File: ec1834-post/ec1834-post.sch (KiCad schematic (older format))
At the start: 15 parts

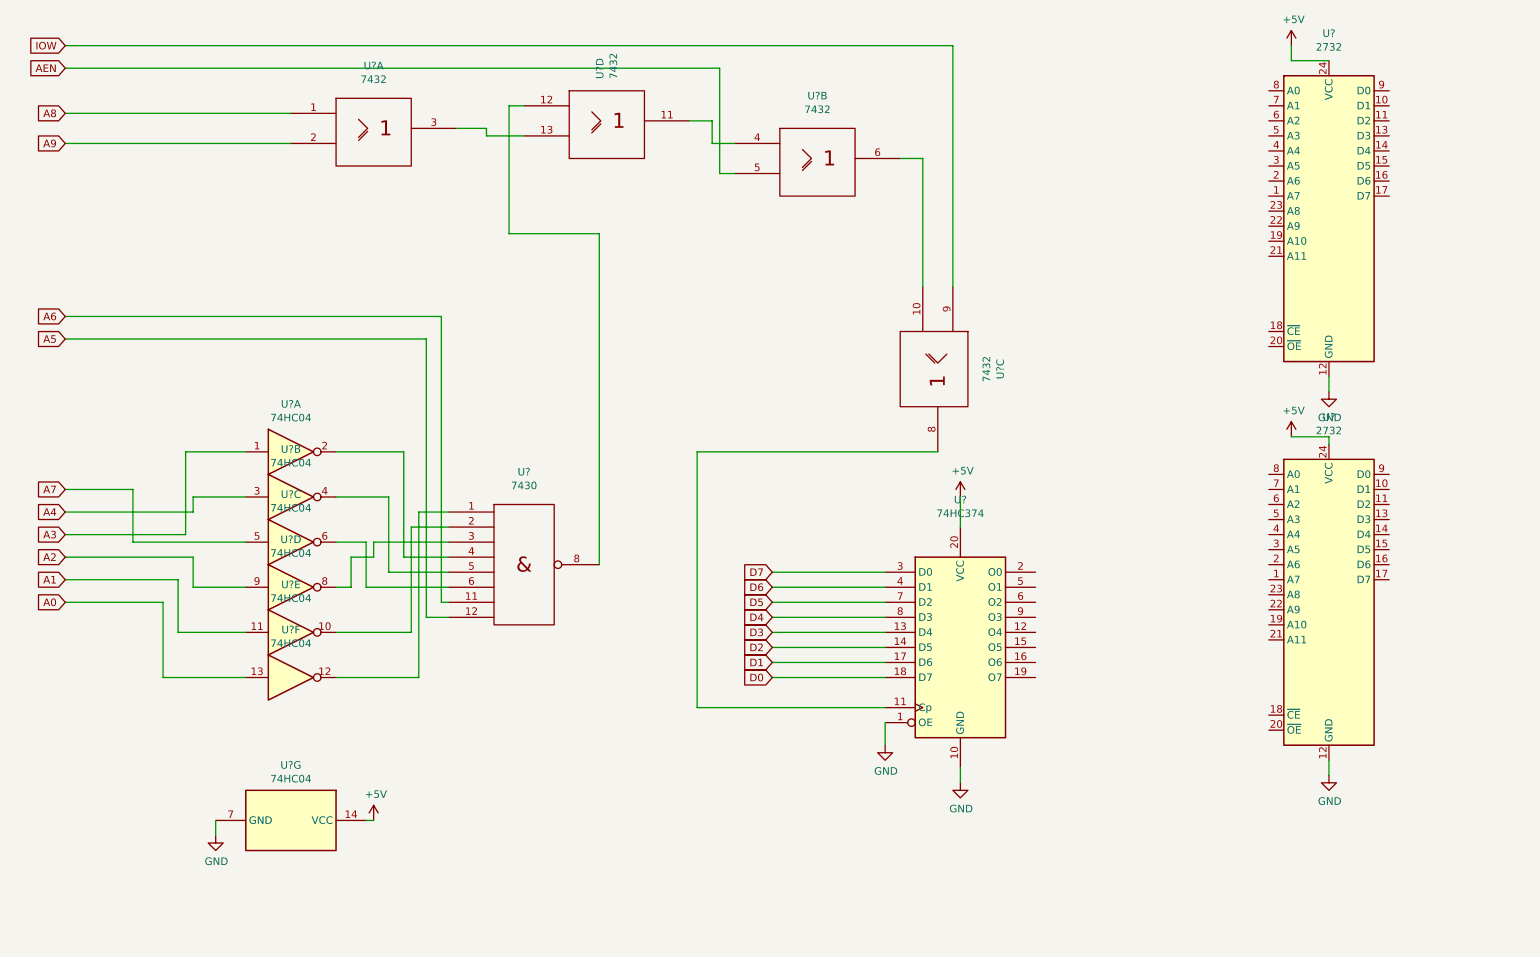
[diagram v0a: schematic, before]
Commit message: Schema completed Building PCB...
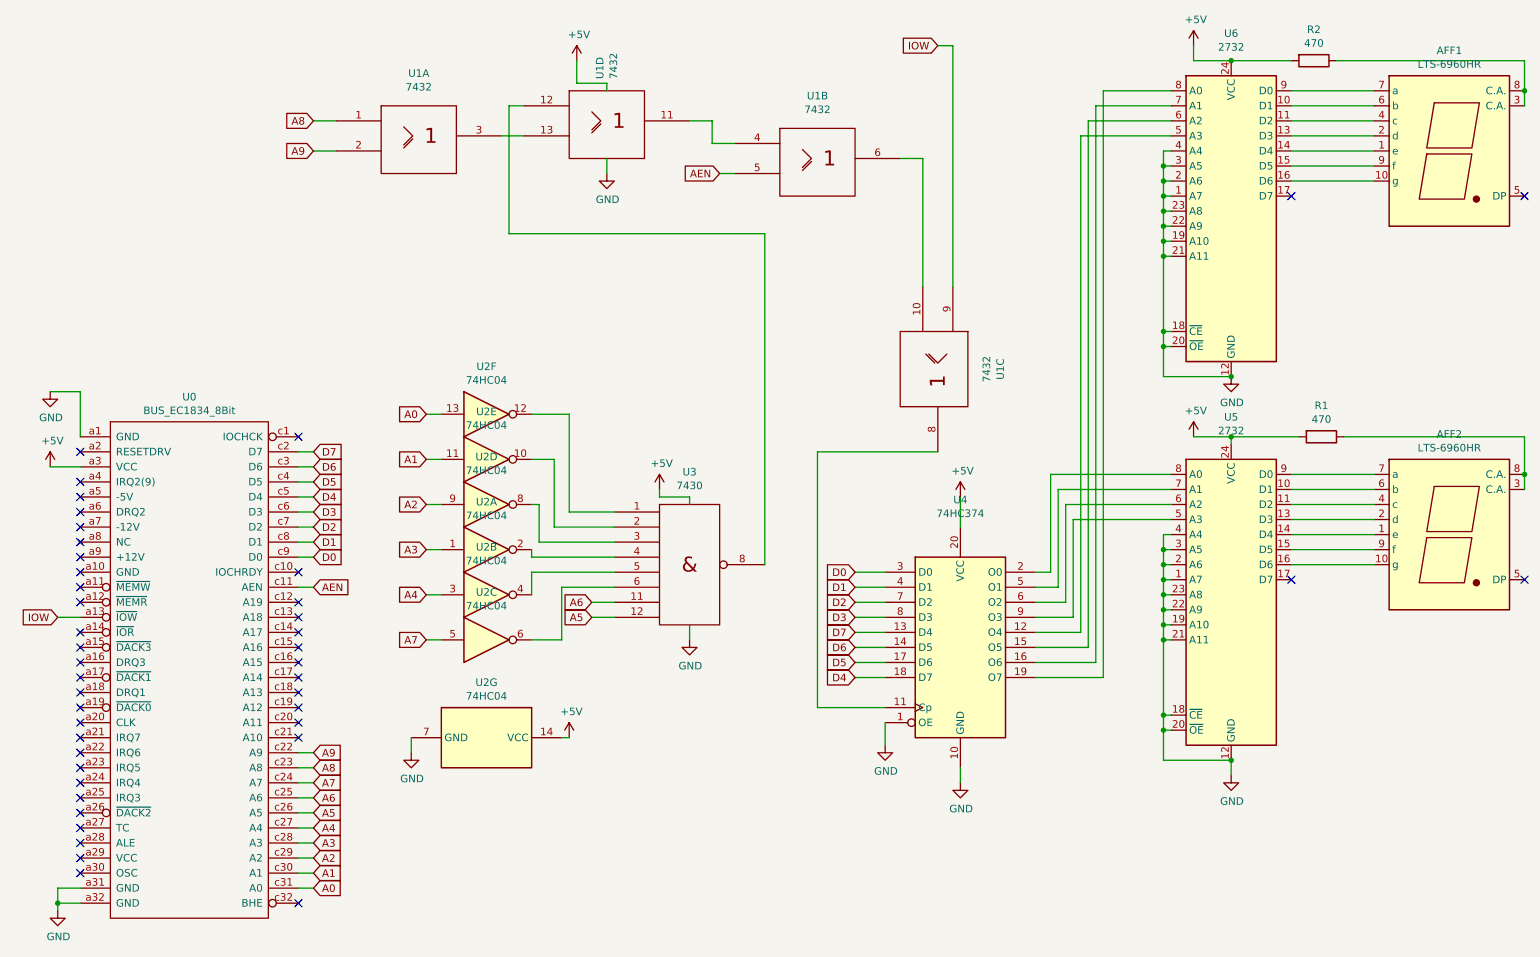
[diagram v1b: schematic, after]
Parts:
- added AFF1, AFF2: LTS-6960HR, Display_7Segment:7SegmentLED_LTS6760_LTS6780, symbol Display_Character:LTS-6960HR
- added R1, R2: 470, Resistor_THT:R_Axial_DIN0309_L9.0mm_D3.2mm_P12.70mm_Horizontal, symbol Device:R
- added U0: BUS_EC1834_8Bit, Connector_DIN:DIN41612_C_2x32_Male_Horizontal_THT, symbol ec1834-post-lib:BUS_EC1834_8Bit
- U1, U2, U3: renamed from U?; footprint (none) -> Package_DIP:DIP-14_W10.16mm
- U4: renamed from U?; footprint (none) -> Package_DIP:DIP-20_W7.62mm
- gave numbers to parts that had none: 2
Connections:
- net Gnd is gone; now on net GND: U1.7 (Gnd), U1.7 (Gnd), U1.7 (Gnd), U1.7 (Gnd), U3.7 (Gnd)
- net Vcc is gone; now on net +5V: U1.14 (Vcc), U1.14 (Vcc), U1.14 (Vcc), U1.14 (Vcc), U3.14 (Vcc)
- net +5V: now also R1.2, R2.2, U0.a3 (VCC)
- net A0: now also U0.c31 (A0)
- net A1: now also U0.c30 (A1)
- net A2: now also U0.c29 (A2)
- net A3: now also U0.c28 (A3)
- net A4: now also U0.c27 (A4)
- net A5: now also U0.c26 (A5)
- net A6: now also U0.c25 (A6)
- net A7: now also U0.c24 (A7)
- net A8: now also U0.c23 (A8)
- net A9: now also U0.c22 (A9)
- net AEN: now also U0.c11 (AEN)
- net D0: now also U4.3 (D0), U0.c9 (D0); no longer U4.18 (D7)
- net D1: now also U4.4 (D1), U0.c8 (D1); no longer U4.17 (D6)
- net D2: now also U4.7 (D2), U0.c7 (D2); no longer U4.14 (D5)
- net D3: now also U4.8 (D3), U0.c6 (D3); no longer U4.13 (D4)
- net D4: now also U4.18 (D7), U0.c5 (D4); no longer U4.8 (D3)
- net D5: now also U4.17 (D6), U0.c4 (D5); no longer U4.7 (D2)
- net D6: now also U4.14 (D5), U0.c3 (D6); no longer U4.4 (D1)
- net D7: now also U4.13 (D4), U0.c2 (D7); no longer U4.3 (D0)
- net GND: now also U5.1 (A7), U5.18 (~CE), U5.19 (A10), U5.2 (A6), U5.20 (~OE), U5.21 (A11), U5.22 (A9), U5.23 (A8), U5.3 (A5), U5.4 (A4), U6.1 (A7), U6.18 (~CE), U6.19 (A10), U6.2 (A6), U6.20 (~OE), U6.21 (A11), U6.22 (A9), U6.23 (A8), U6.3 (A5), U6.4 (A4), U0.a1 (GND), U0.a31 (GND), U0.a32 (GND)
- net IOW: now also U0.a13 (~IOW)
- net at U4.12 (O4): now also U6.5 (A3)
- net at U4.15 (O5): now also U6.6 (A2)
- net at U4.16 (O6): now also U6.7 (A1)
- net at U4.19 (O7): now also U6.8 (A0)
- net at U4.2 (O0): now also U5.8 (A0)
- net at U4.5 (O1): now also U5.7 (A1)
- net at U4.6 (O2): now also U5.6 (A2)
- net at U4.9 (O3): now also U5.5 (A3)
- net at U6.10 (D1): now also AFF1.6 (b)
- net at U6.11 (D2): now also AFF1.4 (c)
- net at U6.13 (D3): now also AFF1.2 (d)
- net at U6.14 (D4): now also AFF1.1 (e)
- net at U6.15 (D5): now also AFF1.9 (f)
- net at U6.16 (D6): now also AFF1.10 (g)
- net at U6.9 (D0): now also AFF1.7 (a)
- net at U5.10 (D1): now also AFF2.6 (b)
- net at U5.11 (D2): now also AFF2.4 (c)
- net at U5.13 (D3): now also AFF2.2 (d)
- net at U5.14 (D4): now also AFF2.1 (e)
- net at U5.15 (D5): now also AFF2.9 (f)
- net at U5.16 (D6): now also AFF2.10 (g)
- net at U5.9 (D0): now also AFF2.7 (a)
- new net: AFF2.3 (C.A.), AFF2.8 (C.A.), R1.1
- new net: AFF1.3 (C.A.), AFF1.8 (C.A.), R2.1
- no-connect marks 0 -> 44
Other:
- moved on the sheet: U1A, U2A, U2B, U2C, U2D, U2E, U2F, U2G, U3, U5, U6

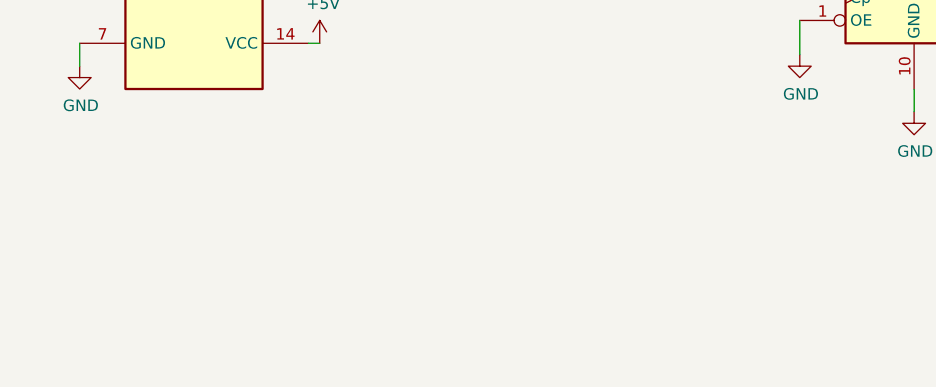
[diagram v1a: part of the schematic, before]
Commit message: Rework from CNC layout (which would be too close for 3018) to better layout for JLCPCB
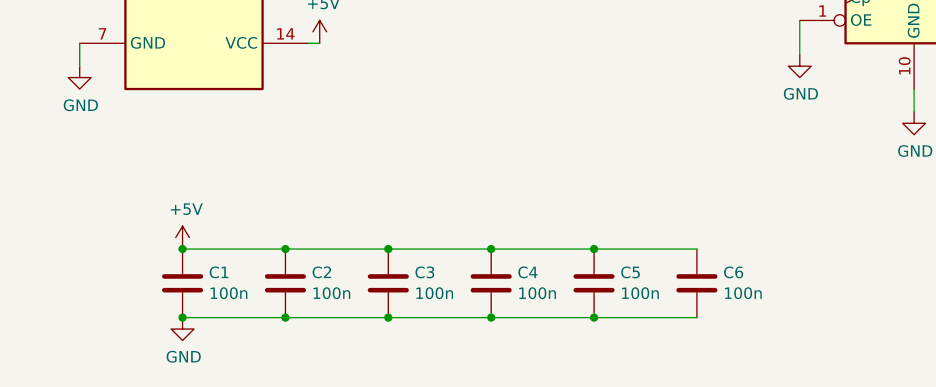
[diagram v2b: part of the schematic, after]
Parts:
- added C1, C2, C3: 100n, Capacitor_THT:C_Axial_L3.8mm_D2.6mm_P7.50mm_Horizontal, symbol Device:C
- added C4: 100n, Capacitor_THT:C_Axial_L5.1mm_D3.1mm_P7.50mm_Horizontal, symbol Device:C
- added C5, C6: 100n, Capacitor_THT:C_Axial_L5.1mm_D3.1mm_P10.00mm_Horizontal, symbol Device:C
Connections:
- net +5V: now also C1.1, C2.1, C3.1, C4.1, C5.1, C6.1
- net GND: now also C1.2, C2.2, C3.2, C4.2, C5.2, C6.2
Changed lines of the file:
@@
 Wire Wire Line
 	4900 5050 4900 5150
+$Comp
+L Device:C C1
+U 1 1 6249EDEF
+P 3500 6850
+F 0 "C1" H 3615 6896 50  0000 L CNN
+F 1 "100n" H 3615 6805 50  0000 L CNN
+F 2 "Capacitor_THT:C_Axial_L3.8mm_D2.6mm_P7.50mm_Horizontal" H 3538 6700 50  0001 C CNN
+F 3 "~" H 3500 6850 50  0001 C CNN
+	1    3500 6850
+	1    0    0    -1
+$EndComp
+$Comp
+L power:+5V #PWR0117
+U 1 1 624A05C0
+P 3500 6700
+F 0 "#PWR0117" H 3500 6550 50  0001 C CNN
+F 1 "+5V" H 3515 6873 50  0000 C CNN
+F 2 "" H 3500 6700 50  0001 C CNN
+F 3 "" H 3500 6700 50  0001 C CNN
+	1    3500 6700
+	1    0    0    -1
+$EndComp
+$Comp
+L power:GND #PWR0118
+U 1 1 624A0F3C
+P 3500 7000
+F 0 "#PWR0118" H 3500 6750 50  0001 C CNN
+F 1 "GND" H 3505 6827 50  0000 C CNN
+F 2 "" H 3500 7000 50  0001 C CNN
+F 3 "" H 3500 7000 50  0001 C CNN
+	1    3500 7000
+	1    0    0    -1
+$EndComp
+$Comp
+L Device:C C2
+U 1 1 624B6BC5
+P 3950 6850
+F 0 "C2" H 4065 6896 50  0000 L CNN
+F 1 "100n" H 4065 6805 50  0000 L CNN
+F 2 "Capacitor_THT:C_Axial_L3.8mm_D2.6mm_P7.50mm_Horizontal" H 3988 6700 50  0001 C CNN
+F 3 "~" H 3950 6850 50  0001 C CNN
+	1    3950 6850
+	1    0    0    -1
+$EndComp
+$Comp
+L Device:C C3
+U 1 1 624B6F52
+P 4400 6850
+F 0 "C3" H 4515 6896 50  0000 L CNN
+F 1 "100n" H 4515 6805 50  0000 L CNN
+F 2 "Capacitor_THT:C_Axial_L3.8mm_D2.6mm_P7.50mm_Horizontal" H 4438 6700 50  0001 C CNN
+F 3 "~" H 4400 6850 50  0001 C CNN
+	1    4400 6850
+	1    0    0    -1
+$EndComp
+$Comp
+L Device:C C4
+U 1 1 624B747C
+P 4850 6850
+F 0 "C4" H 4965 6896 50  0000 L CNN
+F 1 "100n" H 4965 6805 50  0000 L CNN
+F 2 "Capacitor_THT:C_Axial_L5.1mm_D3.1mm_P7.50mm_Horizontal" H 4888 6700 50  0001 C CNN
+F 3 "~" H 4850 6850 50  0001 C CNN
+	1    4850 6850
+	1    0    0    -1
+$EndComp
+$Comp
+L Device:C C5
+U 1 1 624B78D5
+P 5300 6850
+F 0 "C5" H 5415 6896 50  0000 L CNN
+F 1 "100n" H 5415 6805 50  0000 L CNN
+F 2 "Capacitor_THT:C_Axial_L5.1mm_D3.1mm_P10.00mm_Horizontal" H 5338 6700 50  0001 C CNN
+F 3 "~" H 5300 6850 50  0001 C CNN
+	1    5300 6850
+	1    0    0    -1
+$EndComp
+$Comp
+L Device:C C6
+U 1 1 624B7CA9
+P 5750 6850
+F 0 "C6" H 5865 6896 50  0000 L CNN
+F 1 "100n" H 5865 6805 50  0000 L CNN
+F 2 "Capacitor_THT:C_Axial_L5.1mm_D3.1mm_P10.00mm_Horizontal" H 5788 6700 50  0001 C CNN
+F 3 "~" H 5750 6850 50  0001 C CNN
+	1    5750 6850
+	1    0    0    -1
+$EndComp
+Wire Wire Line
+	3500 6700 3950 6700
+Connection ~ 3500 6700
+Wire Wire Line
+	3950 6700 4400 6700
+Connection ~ 3950 6700
+Wire Wire Line
+	4400 6700 4850 6700
+Connection ~ 4400 6700
+Wire Wire Line
+	4850 6700 5300 6700
+Connection ~ 4850 6700
+Wire Wire Line
+	5300 6700 5750 6700
+Connection ~ 5300 6700
+Wire Wire Line
+	3500 7000 3950 7000
+Connection ~ 3500 7000
+Wire Wire Line
+	3950 7000 4400 7000
+Connection ~ 3950 7000
+Wire Wire Line
+	4400 7000 4850 7000
+Connection ~ 4400 7000
+Wire Wire Line
+	4850 7000 5300 7000
+Connection ~ 4850 7000
+Wire Wire Line
+	5300 7000 5750 7000
+Connection ~ 5300 7000
 $EndSCHEMATC
